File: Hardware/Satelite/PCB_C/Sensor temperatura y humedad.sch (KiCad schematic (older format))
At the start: 2 parts

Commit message: Cambio en el simbolo de SW1 en PCB_A
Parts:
- C?: footprint (none) -> Capacitor_SMD:C_0603_1608Metric_Pad1.05x0.95mm_HandSolder; Manufacturer Part Number (none) -> EMK107B7104KAHT
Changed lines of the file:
@@
 F 0 "C?" H 6992 3496 50  0000 L CNN
 F 1 "100nF" H 6992 3405 50  0000 L CNN
-F 2 "" H 6900 3450 50  0001 C CNN
+F 2 "Capacitor_SMD:C_0603_1608Metric_Pad1.05x0.95mm_HandSolder" H 6900 3450 50  0001 C CNN
 F 3 "~" H 6900 3450 50  0001 C CNN
+F 4 "EMK107B7104KAHT" H 6900 3450 50  0001 C CNN "Manufacturer Part Number"
 	1    6900 3450
 	1    0    0    -1

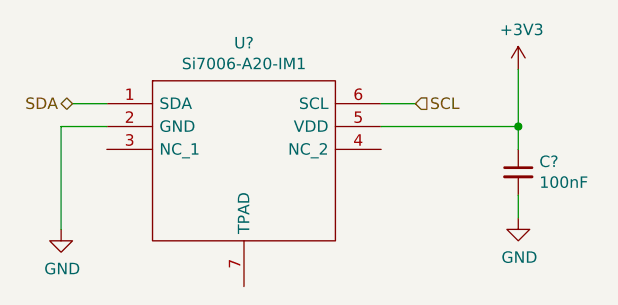
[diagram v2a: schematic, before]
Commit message: Modificaciones en conectores, netlist para PCB C
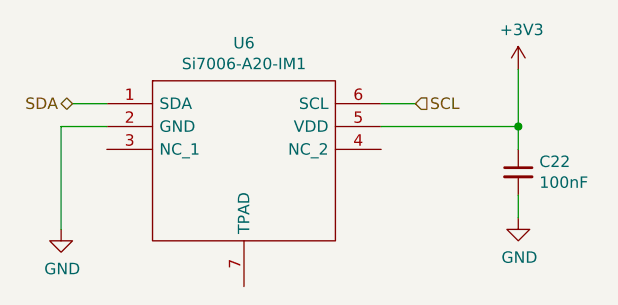
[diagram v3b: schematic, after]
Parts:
- U6: renamed from U?; footprint SON100P300X300X80-7N -> SamacSys_Parts:SON100P300X300X80-7N
- gave numbers to parts that had none: 1
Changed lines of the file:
@@
 $EndDescr
 $Comp
-L SamacSys_Parts:Si7006-A20-IM1 U?
+L SamacSys_Parts:Si7006-A20-IM1 U6
 U 1 1 5BB7134A
 P 5100 3150
-F 0 "U?" H 5700 3415 50  0000 C CNN
+F 0 "U6" H 5700 3415 50  0000 C CNN
 F 1 "Si7006-A20-IM1" H 5700 3324 50  0000 C CNN
-F 2 "SON100P300X300X80-7N" H 6150 3250 50  0001 L CNN
+F 2 "SamacSys_Parts:SON100P300X300X80-7N" H 6150 3250 50  0001 L CNN
 F 3 "https://www.silabs.com/documents/public/data-sheets/Si7006-A20.pdf" H 6150 3150 50  0001 L CNN
 F 4 "Si7006 Digital RH temp sensor w filter Silicon Labs Si7006-A20-IM1 Temperature & Humidity Sensor, -40  +125 C, 6-Pin DFN" H 6150 3050 50  0001 L CNN "Description"
@@
 $EndComp
 $Comp
-L Device:C_Small C?
+L Device:C_Small C22
 U 1 1 5BB71601
 P 6900 3450
-F 0 "C?" H 6992 3496 50  0000 L CNN
+F 0 "C22" H 6992 3496 50  0000 L CNN
 F 1 "100nF" H 6992 3405 50  0000 L CNN
 F 2 "Capacitor_SMD:C_0603_1608Metric_Pad1.05x0.95mm_HandSolder" H 6900 3450 50  0001 C CNN
@@
 $EndComp
 $Comp
-L power:+3V3 #PWR?
+L power:+3V3 #PWR067
 U 1 1 5BB716EE
 P 6900 3000
-F 0 "#PWR?" H 6900 2850 50  0001 C CNN
+F 0 "#PWR067" H 6900 2850 50  0001 C CNN
 F 1 "+3V3" H 6915 3173 50  0000 C CNN
 F 2 "" H 6900 3000 50  0001 C CNN
@@
 $EndComp
 $Comp
-L power:GND #PWR?
+L power:GND #PWR068
 U 1 1 5BB71724
 P 6900 3650
-F 0 "#PWR?" H 6900 3400 50  0001 C CNN
+F 0 "#PWR068" H 6900 3400 50  0001 C CNN
 F 1 "GND" H 6905 3477 50  0000 C CNN
 F 2 "" H 6900 3650 50  0001 C CNN
@@
 	6900 3650 6900 3550
 $Comp
-L power:GND #PWR?
+L power:GND #PWR066
 U 1 1 5BB717C2
 P 4900 3700
-F 0 "#PWR?" H 4900 3450 50  0001 C CNN
+F 0 "#PWR066" H 4900 3450 50  0001 C CNN
 F 1 "GND" H 4905 3527 50  0000 C CNN
 F 2 "" H 4900 3700 50  0001 C CNN

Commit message: Capacitores 0402 para PCB_C
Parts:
- C22: footprint Capacitor_SMD:C_0603_1608Metric_Pad1.05x0.95mm_HandSolder -> Capacitor_SMD:C_0402_1005Metric; Manufacturer Part Number EMK107B7104KAHT -> GCM155R71C104KA55D
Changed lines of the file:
@@
 F 0 "C22" H 6992 3496 50  0000 L CNN
 F 1 "100nF" H 6992 3405 50  0000 L CNN
-F 2 "Capacitor_SMD:C_0603_1608Metric_Pad1.05x0.95mm_HandSolder" H 6900 3450 50  0001 C CNN
+F 2 "Capacitor_SMD:C_0402_1005Metric" H 6900 3450 50  0001 C CNN
 F 3 "~" H 6900 3450 50  0001 C CNN
-F 4 "EMK107B7104KAHT" H 6900 3450 50  0001 C CNN "Manufacturer Part Number"
+F 4 "GCM155R71C104KA55D" H 6900 3450 50  0001 C CNN "Manufacturer Part Number"
 	1    6900 3450
 	1    0    0    -1

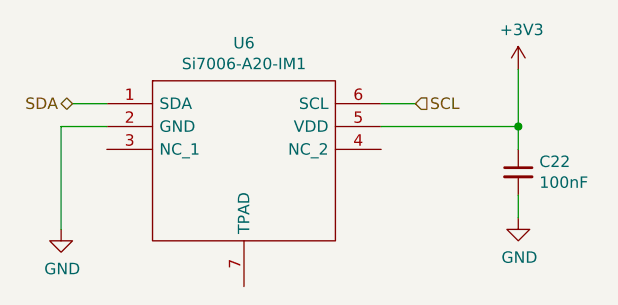
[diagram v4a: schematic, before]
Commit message: Uso de 3.3V internos para todos los sensores en PCB_C y agregado de divisor resistivo para la señal de 5V proveniente del BQ24392.
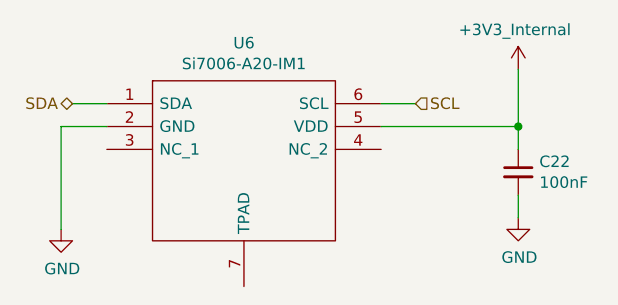
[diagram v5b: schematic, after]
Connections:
- net +3V3 renamed +3V3_Internal
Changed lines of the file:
@@
-$EndComp
-$Comp
-L power:+3V3 #PWR067
-U 1 1 5BB716EE
-P 6900 3000
-F 0 "#PWR067" H 6900 2850 50  0001 C CNN
-F 1 "+3V3" H 6915 3173 50  0000 C CNN
-F 2 "" H 6900 3000 50  0001 C CNN
-F 3 "" H 6900 3000 50  0001 C CNN
-	1    6900 3000
-	1    0    0    -1
 $EndComp
 $Comp
@@
 Wire Wire Line
 	6300 3150 6450 3150
+$Comp
+L AXTEC_IC:+3V3_Internal #PWR?
+U 1 1 5C5DE6F7
+P 6900 3000
+AR Path="/5C5DE6F7" Ref="#PWR?"  Part="1"
+AR Path="/5BB122CA/5C5DE6F7" Ref="#PWR18"  Part="1"
+F 0 "#PWR18" H 6900 3400 50  0001 C CNN
+F 1 "+3V3_Internal" H 6885 3173 50  0000 C CNN
+F 2 "" H 6900 3000 50  0001 C CNN
+F 3 "" H 6900 3000 50  0001 C CNN
+	1    6900 3000
+	1    0    0    -1
+$EndComp
 $EndSCHEMATC
